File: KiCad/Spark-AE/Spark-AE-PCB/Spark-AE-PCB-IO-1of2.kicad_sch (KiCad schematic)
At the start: 36 parts, among them J4 Inputs, J5 Outputs, U4 MCP6002T-I_MS, U5 MCP6002T-I_MS

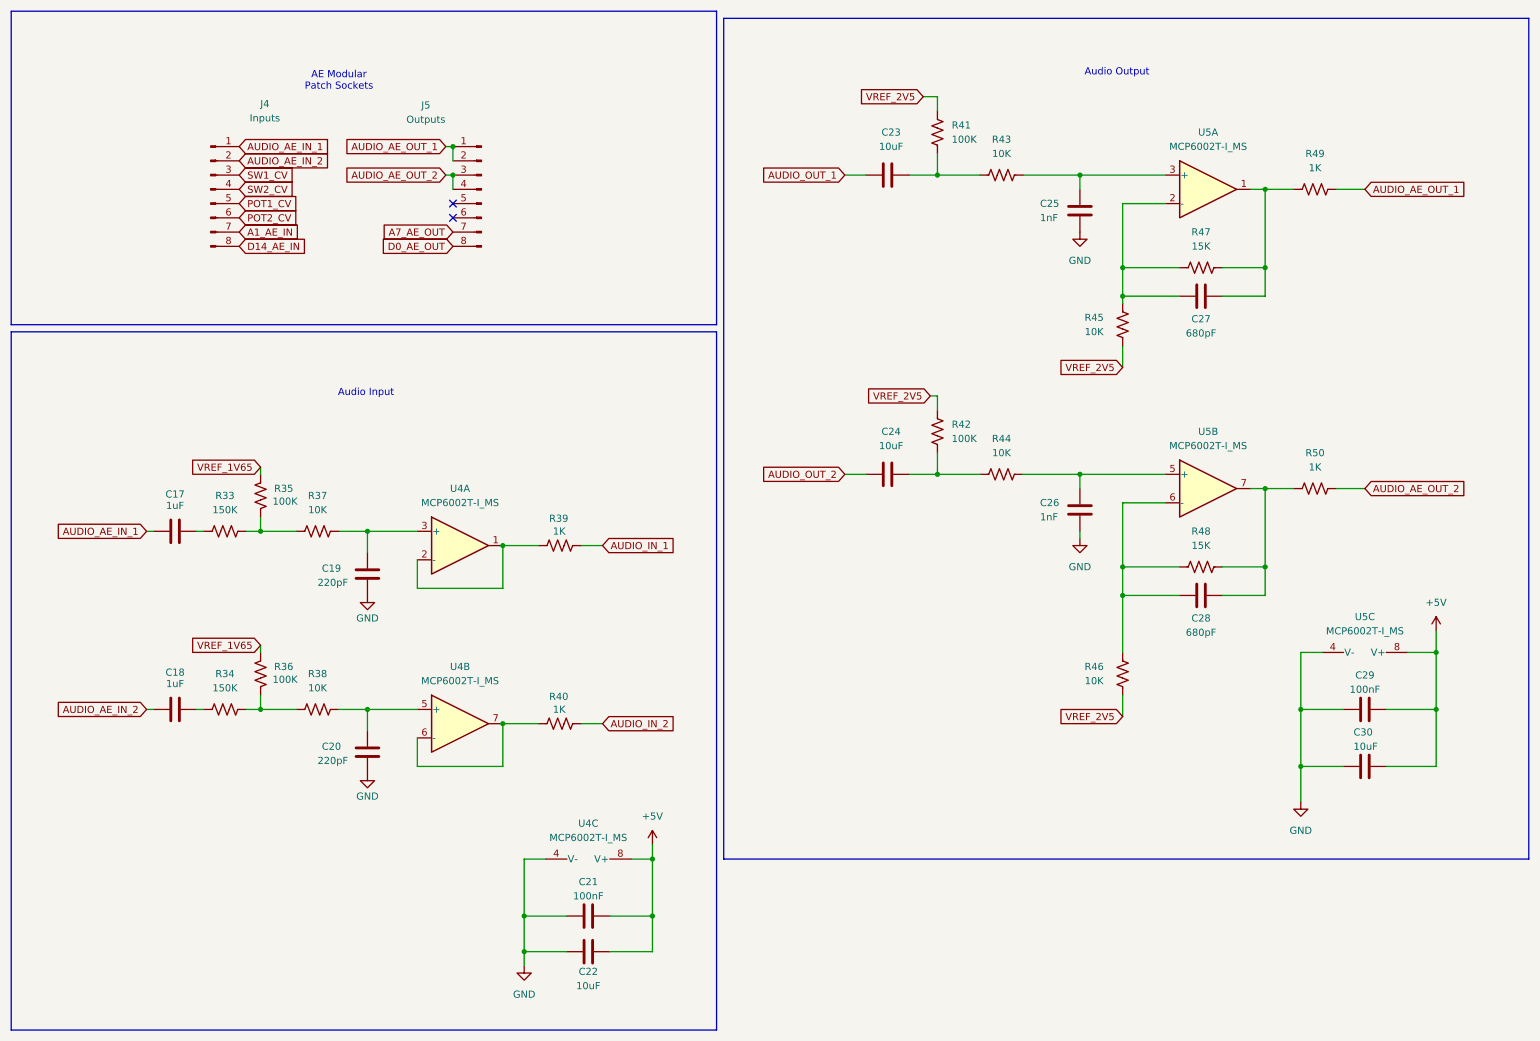
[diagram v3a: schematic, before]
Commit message: pcb layout complete. ready for final pre-fab confirmation.
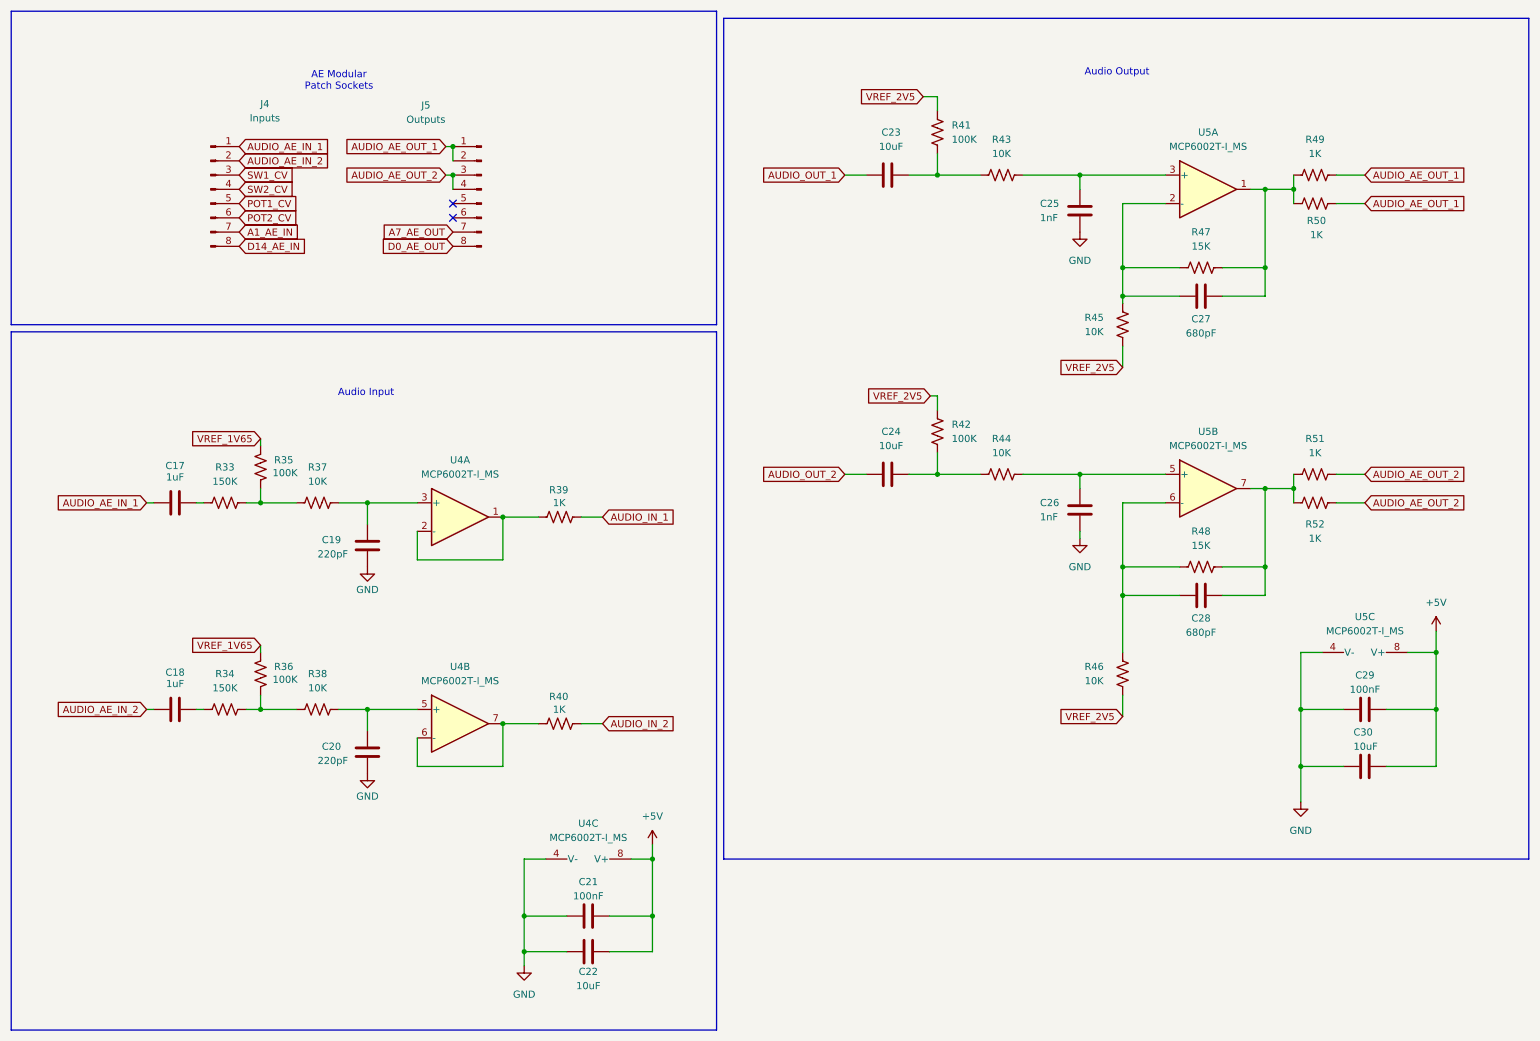
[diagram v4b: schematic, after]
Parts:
- added R50, R52: 1K, Resistor_SMD:R_0603_1608Metric, symbol Device:R_US
- renumbered R50 to R51
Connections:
- net AUDIO_AE_OUT_1: now also R50.2
- net AUDIO_AE_OUT_2: now also R52.2
- net at C28.1, R48.2, R51.1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: now also R52.1
- net at C27.1, R47.2, R49.1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: now also R50.1
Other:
- moved on the sheet: C17, C19, R33, R35, R37, R39, R49, R51, U4A
